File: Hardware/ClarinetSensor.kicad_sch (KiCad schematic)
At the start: 28 parts, among them J1 USB_C_Receptacle_USB2.0_16P, J2 Conn_01x02, J3 Conn_01x04, J4 Conn_01x04, SW1 SW_Push, SW2 SW_Push, U1 MCP73831-2-OT, U2 AP2112K-3.3, U3 ESP32-C3-WROOM-02

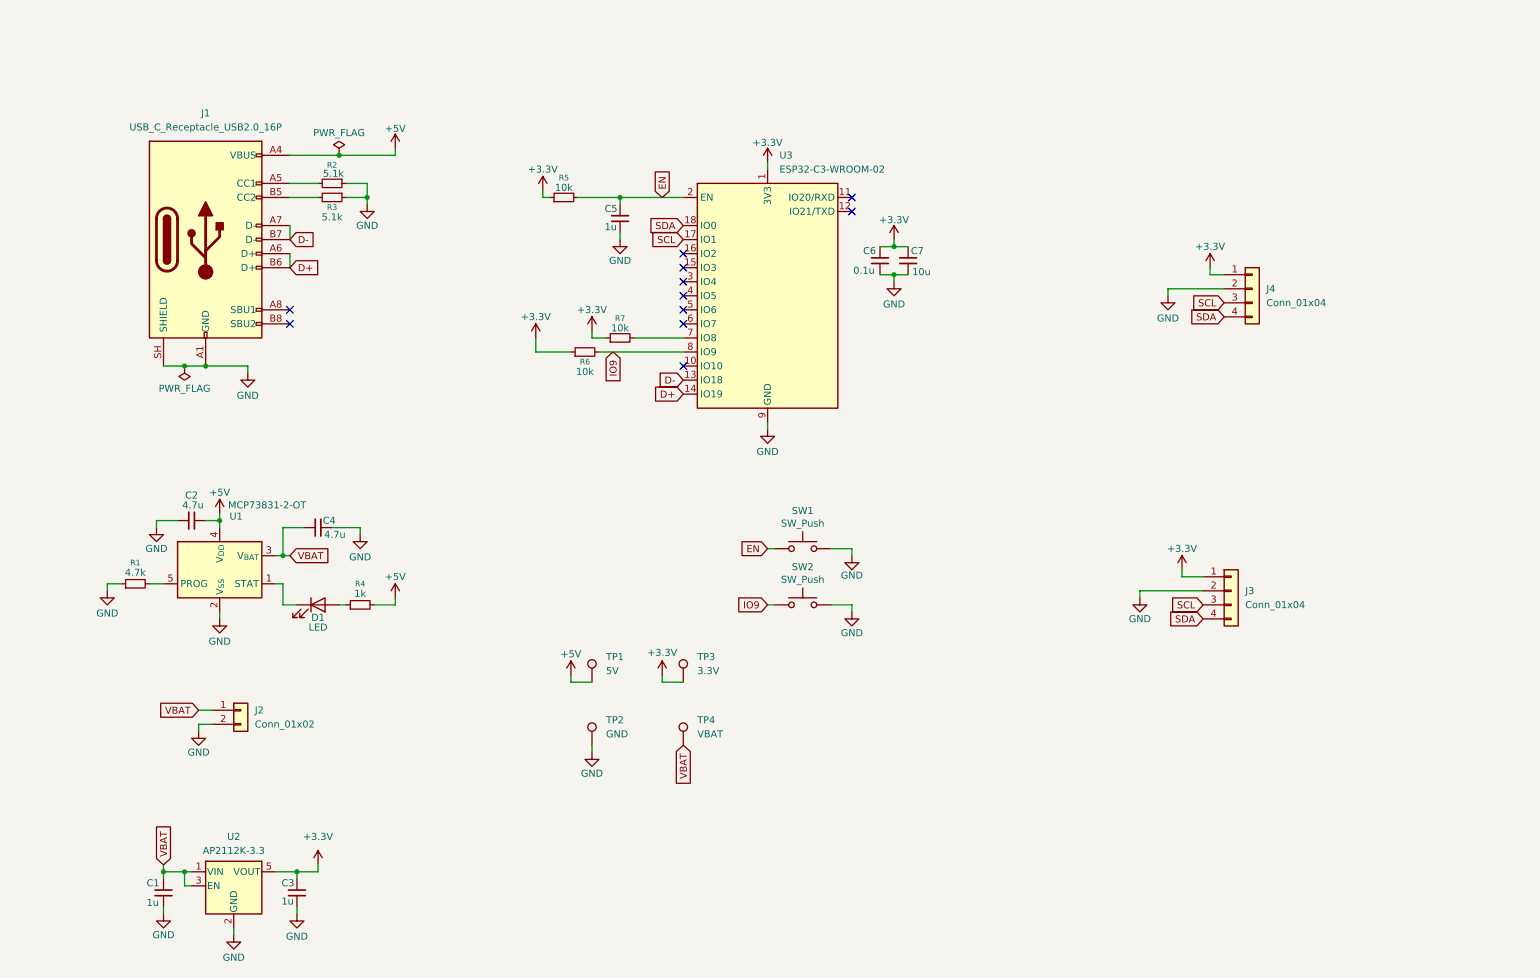
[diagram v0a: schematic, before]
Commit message: Changed the polling rate
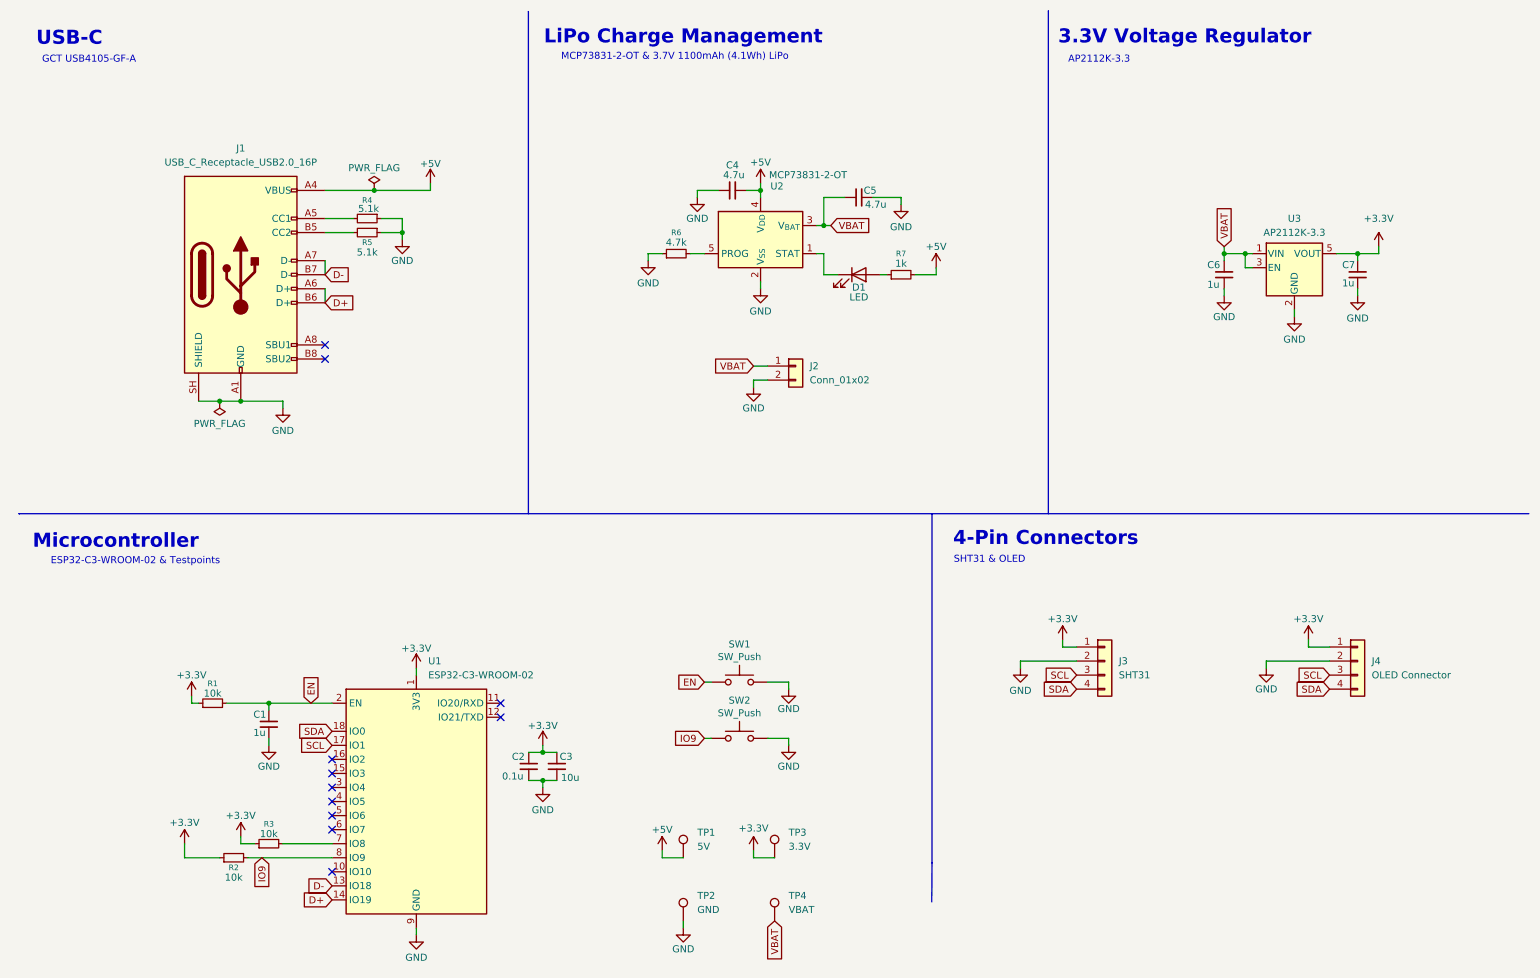
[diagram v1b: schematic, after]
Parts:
- J3: renamed from J4; value Conn_01x04 -> SHT31
- J4: renamed from J3; value Conn_01x04 -> OLED Connector
- renumbered C5 to C1, C6 to C2, C7 to C3, C2 to C4, C4 to C5, C1 to C6, C3 to C7, R5 to R1, R6 to R2, R7 to R3, R2 to R4, R3 to R5, R1 to R6, R4 to R7, U3 to U1, U1 to U2, U2 to U3
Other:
- note added: "3.3V Voltage Regulator"
- note added: "4-Pin Connectors"
- note added: "AP2112K-3.3"
- note added: "ESP32-C3-WROOM-02 & Testpoints"
- note added: "GCT USB4105-GF-A"
- note added: "LiPo Charge Management"
- note added: "MCP73831-2-OT & 3.7V 1100mAh (4.1Wh) LiPo"
- note added: "Microcontroller"
- note added: "SHT31 & OLED"
- note added: "USB-C"
- company: (none) -> Project Files:
- title: (none) -> Clarinet Hygrothermometer
- moved on the sheet: C1, C2, C3, C4, C5, C6, C7, D1, J1, J2, J3, J4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
